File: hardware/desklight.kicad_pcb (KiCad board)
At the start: 2 copper layers, 30 x 30 mm, 10 parts, among them IC1 ATTINY10-TS, P1 AVR_TPI, P2 Pwr5V1500mA, P3 WS2812_CON, SW1 Rotary_Encoder_Switch

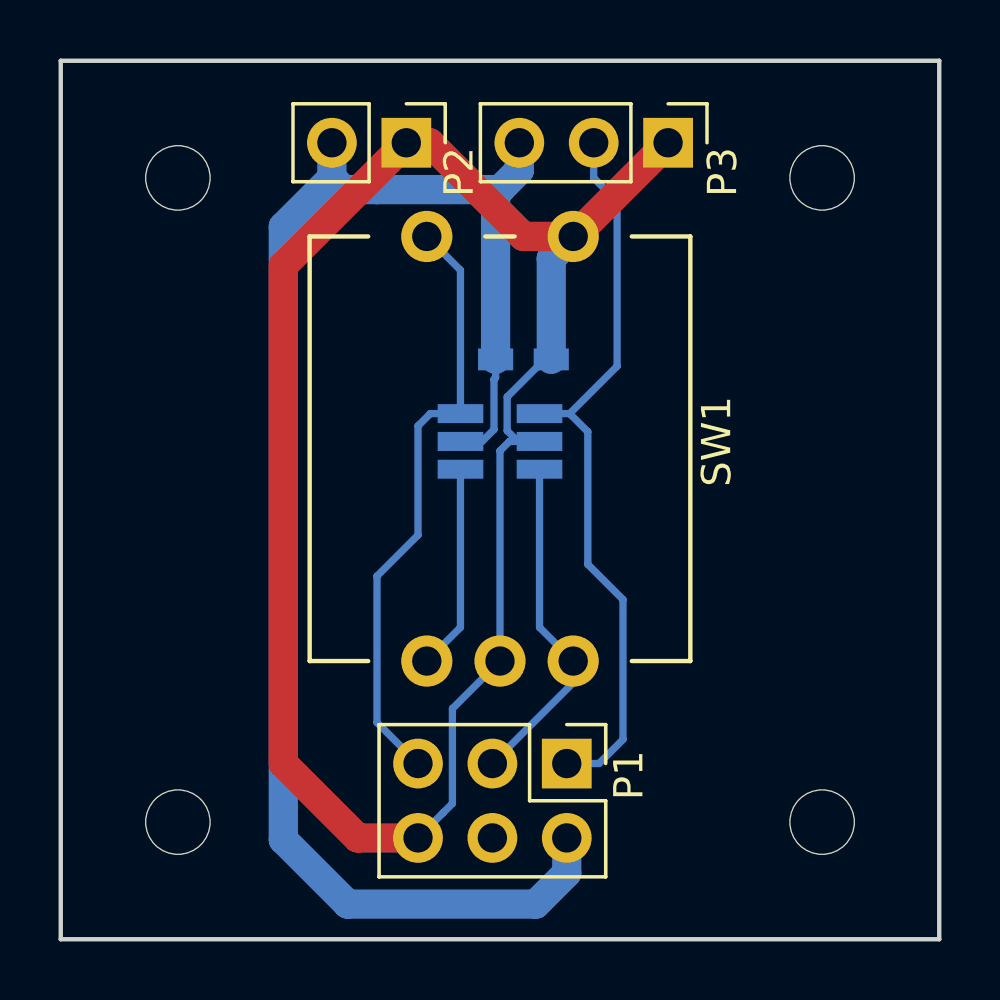
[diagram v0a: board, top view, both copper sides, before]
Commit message: add debouncing caps
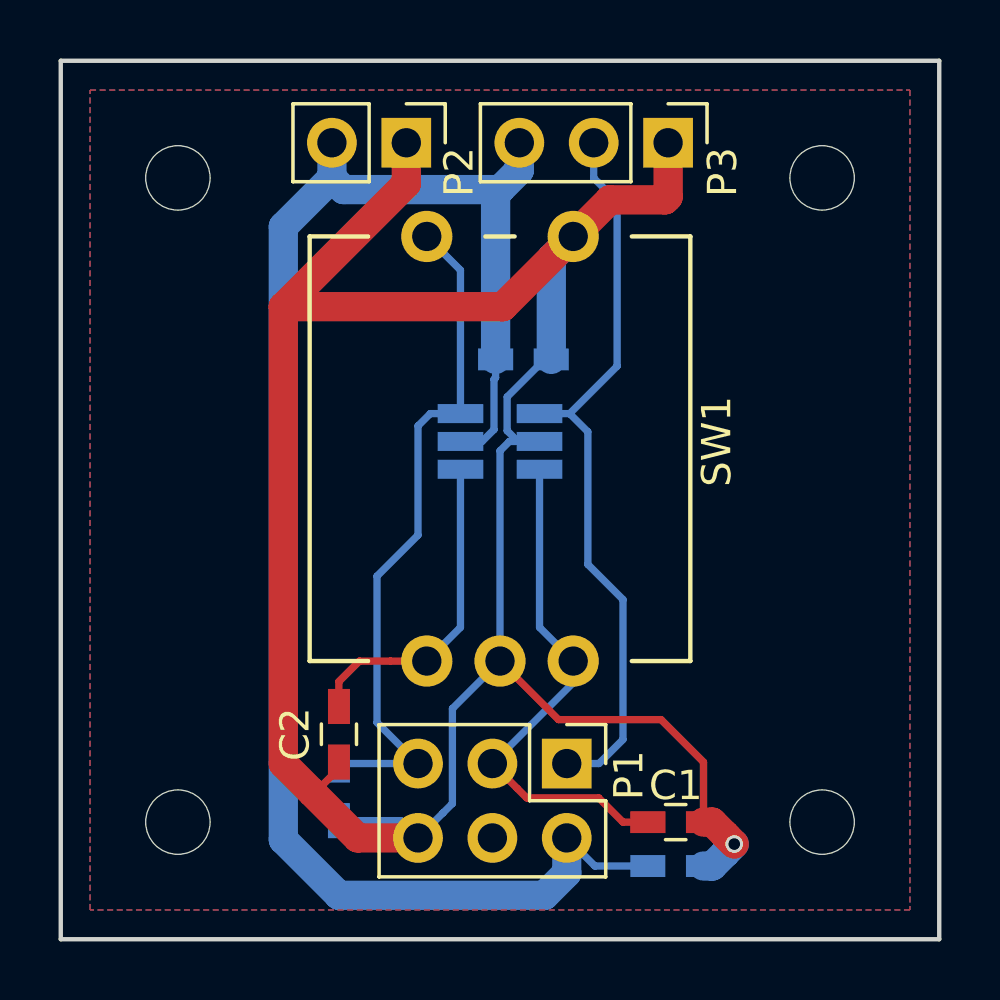
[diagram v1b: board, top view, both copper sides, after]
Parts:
- added C1: C, Capacitors_SMD:C_0603_HandSoldering, F.Cu at (151.0, 106.0)
- added C2: C, Capacitors_SMD:C_0603_HandSoldering, F.Cu at (139.5, 103.0)
- added C3: C, Capacitors_SMD:C_0603_HandSoldering, B.Cu at (139.5, 105.0)
- added C4: 100n, Capacitors_SMD:C_0603_HandSoldering, B.Cu at (151.0, 107.5)
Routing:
- net GND: track 65.0 -> 87.6 mm, vias 0 -> 1
- net /SCK: track 11.7 -> 17.8 mm
- net Net-(C2-Pad1): track 7.03 -> 11.2 mm
- net VCC: track 54.1 -> 57.0 mm
- net /~RESET: track 20.8 -> 23.6 mm
- added copper zone on B.Cu, net GND
- added copper zone on F.Cu, net GND

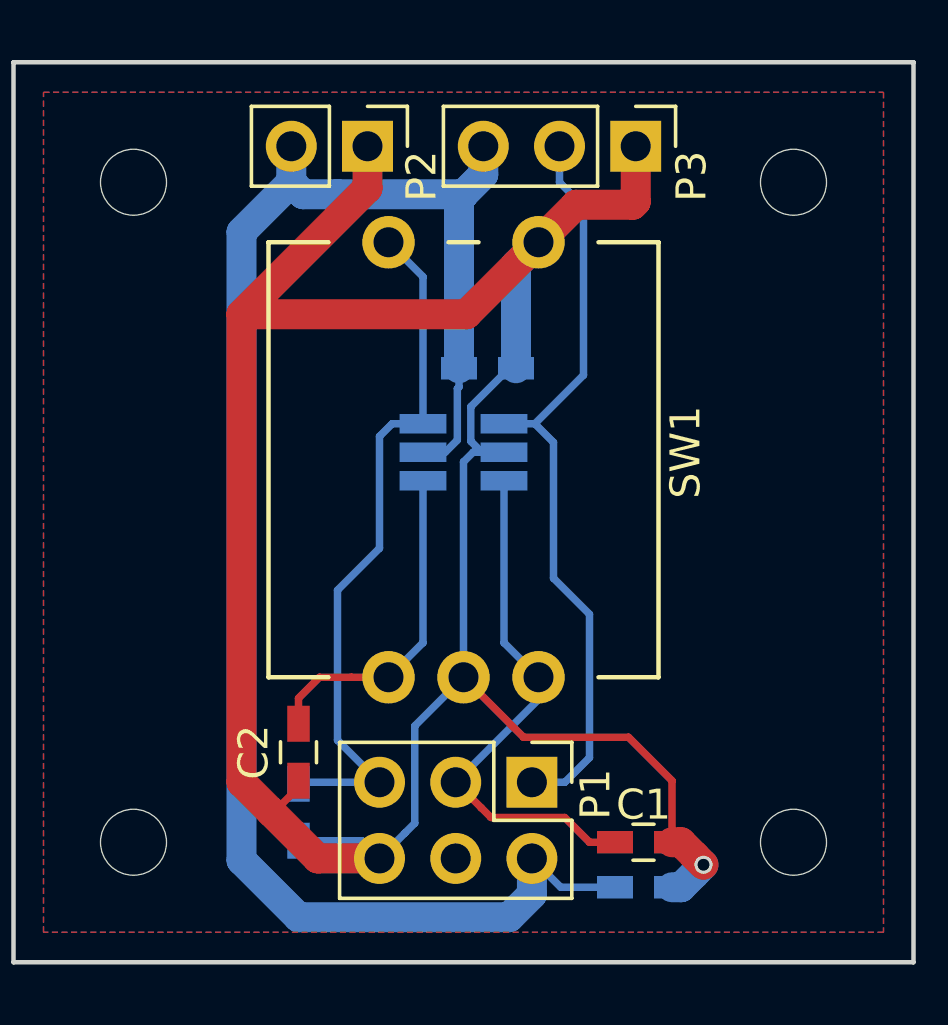
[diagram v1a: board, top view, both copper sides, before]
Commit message: re-routed with cleanup
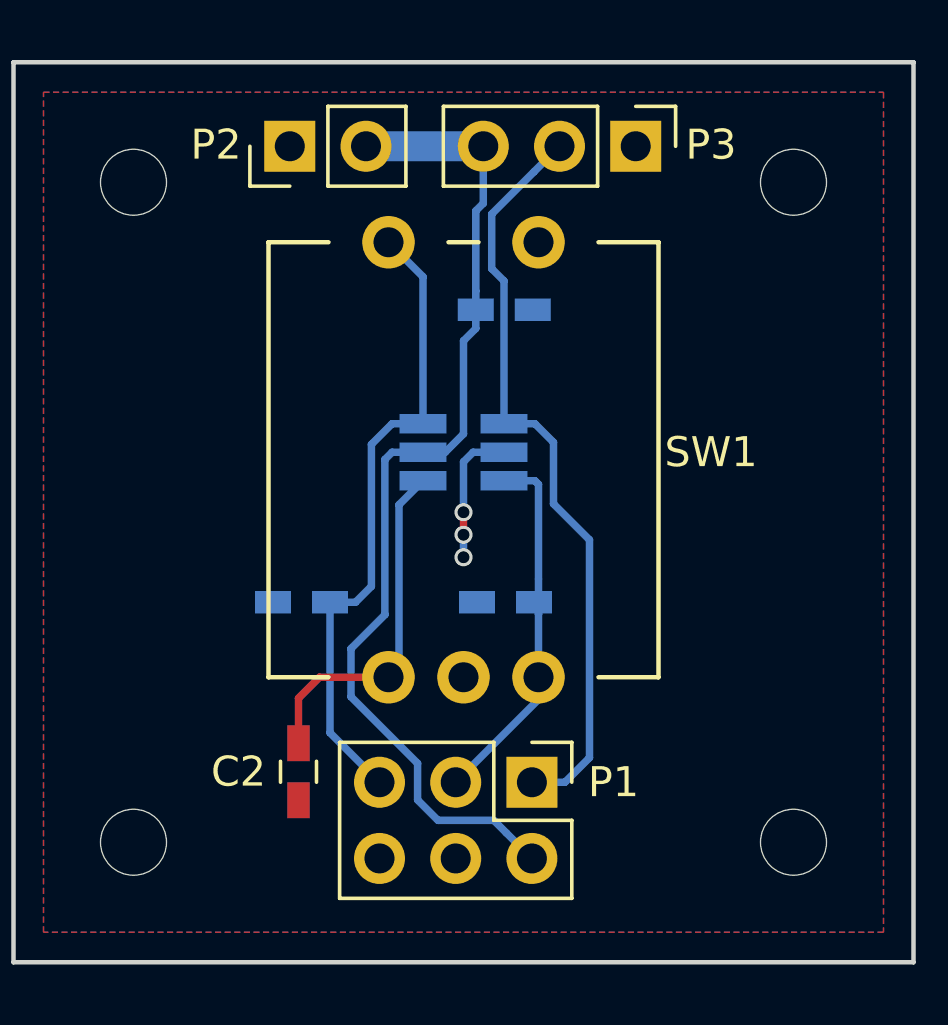
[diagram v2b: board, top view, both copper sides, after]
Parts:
- removed C5: 100n, Capacitors_SMD:C_0603_HandSoldering
- C1: moved to B.Cu
- moved C4 19.8 mm to (146.4, 88.2)
- moved C1 9.23 mm to (146.4, 98.0), turned to 180 degrees
- moved C3 7.00 mm to (139.6, 98.0), turned to 180 degrees
- moved P2 2.59 mm to (139.2, 82.8), turned to 90 degrees
- moved C2 0.65 mm to (139.5, 103.7)
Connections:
- P1 pad 4: Net-(P1-Pad4) -> (no net)
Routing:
- net GND: track 87.6 -> 4.70 mm, vias 1 -> 3
- net VCC: track 57.0 -> 34.1 mm
- net /SCK: track 17.8 -> 12.7 mm
- net /~RESET: track 23.6 -> 21.6 mm
- net Net-(C2-Pad1): track 11.2 -> 11.8 mm

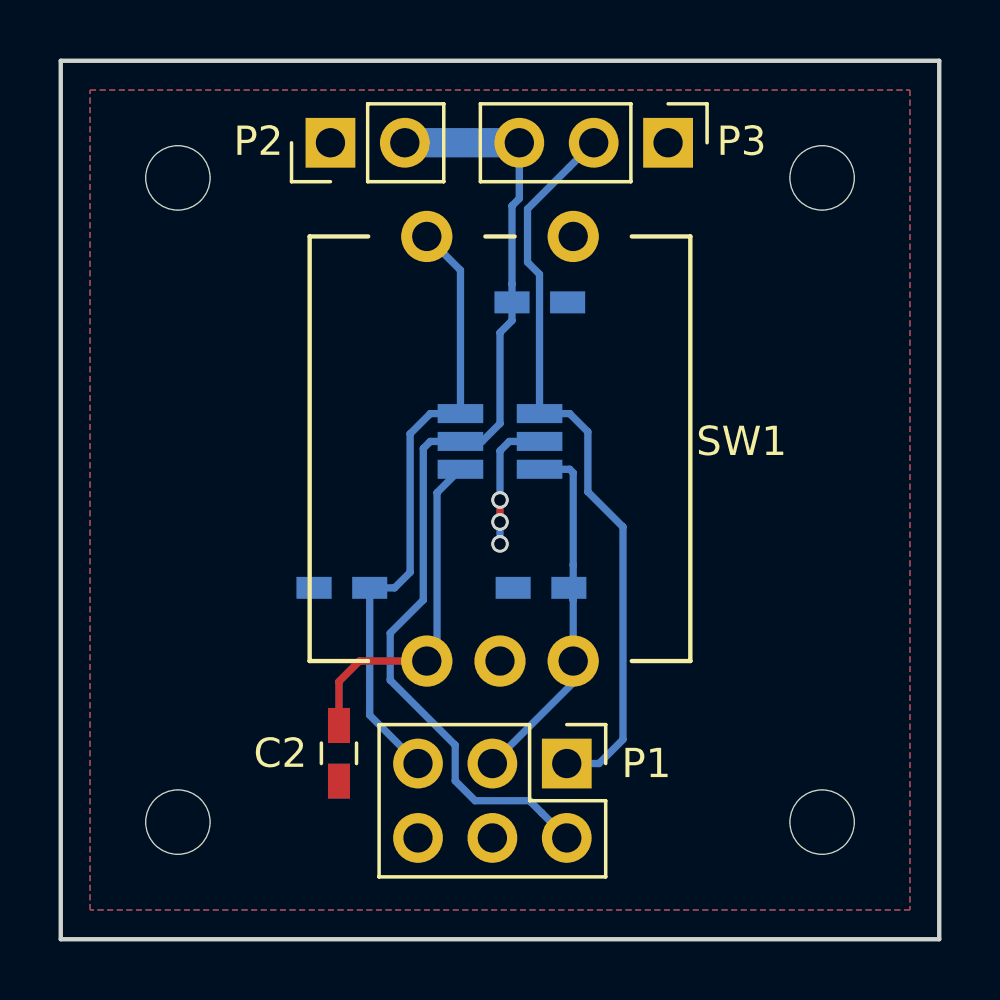
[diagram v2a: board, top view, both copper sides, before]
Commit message: re-route in 2.5x2.5cm formfactor.
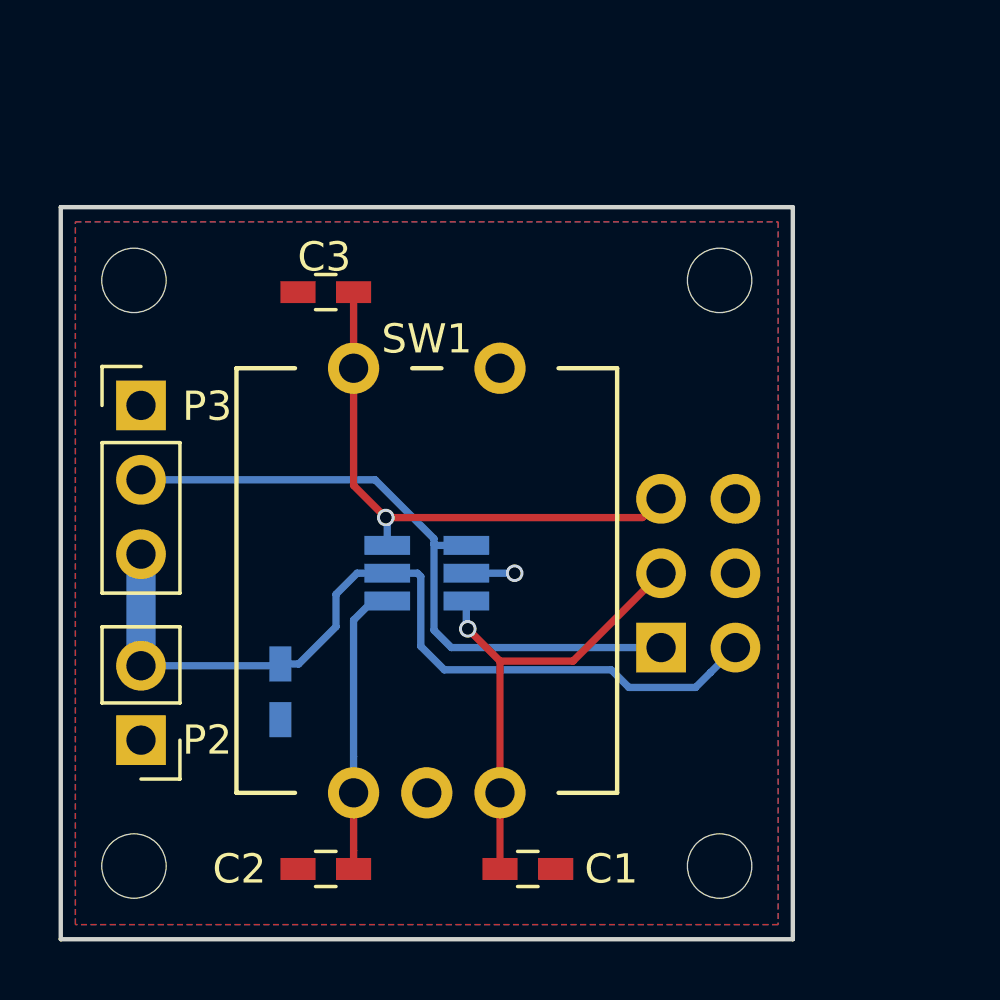
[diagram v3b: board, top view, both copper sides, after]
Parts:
- C1, C3: moved to F.Cu
- P1: moved to B.Cu
- moved P2 21.4 mm to (132.7, 103.2), turned to 180 degrees
- moved P3 20.1 mm to (132.7, 91.8), turned to 0 degrees
- moved C4 16.0 mm to (137.5, 101.5), turned to 270 degrees
- moved C3 10.1 mm to (139.1, 87.9)
- moved C1 9.61 mm to (145.9, 107.6), turned to 0 degrees
- moved IC1 5.15 mm to (142.5, 97.5)
- moved SW1 5.15 mm to (142.5, 97.5)
- moved P1 5.10 mm to (150.5, 100.0), turned to 0 degrees
- moved REF** 4.95 mm to (152.5, 87.5)
- moved C2 3.98 mm to (139.1, 107.6), turned to 180 degrees
- moved REF** 3.81 mm to (152.5, 107.5)
- moved REF** 3.81 mm to (132.5, 87.5)
- moved REF** 2.12 mm to (132.5, 107.5)
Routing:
- net VCC: track 34.1 -> 29.6 mm
- net /SCK: track 12.7 -> 16.8 mm, vias 0 -> 1
- net GND: track 4.70 -> 1.65 mm, vias 3 -> 1
- net /~RESET: track 21.6 -> 18.8 mm, vias 0 -> 1
- net /DOUT: track 25.8 -> 23.1 mm
- net Net-(C2-Pad1): track 11.8 -> 9.92 mm
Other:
- board size 30 x 30 mm -> 25 x 25 mm

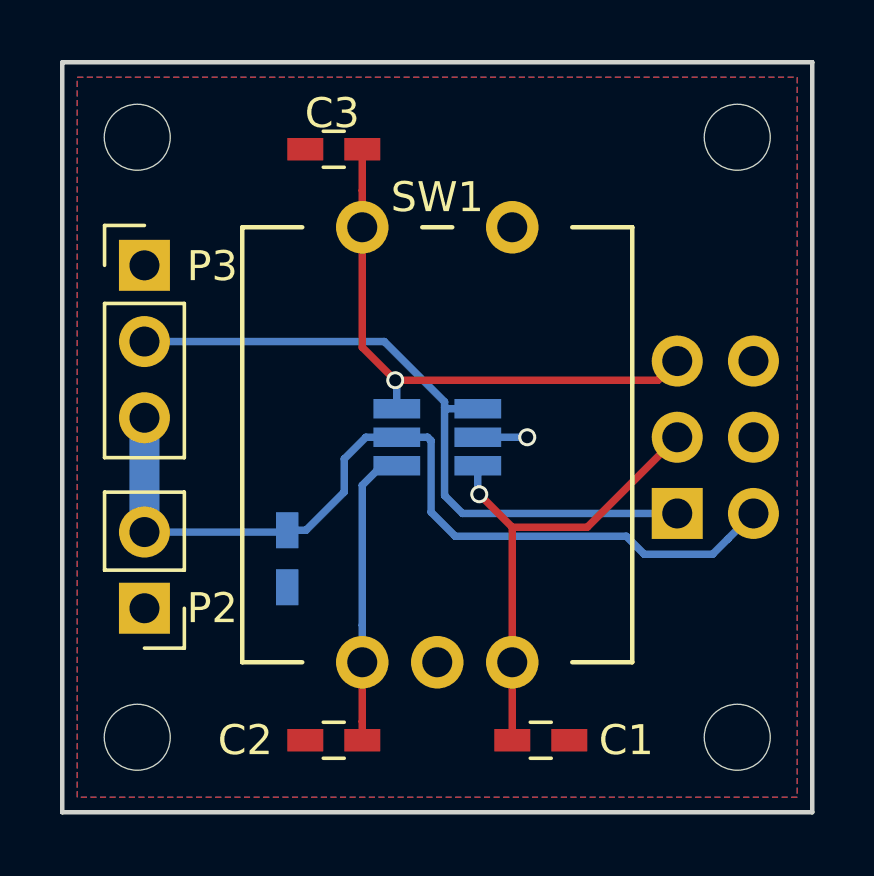
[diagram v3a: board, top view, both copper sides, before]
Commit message: added resistors to allow in-circuit programming
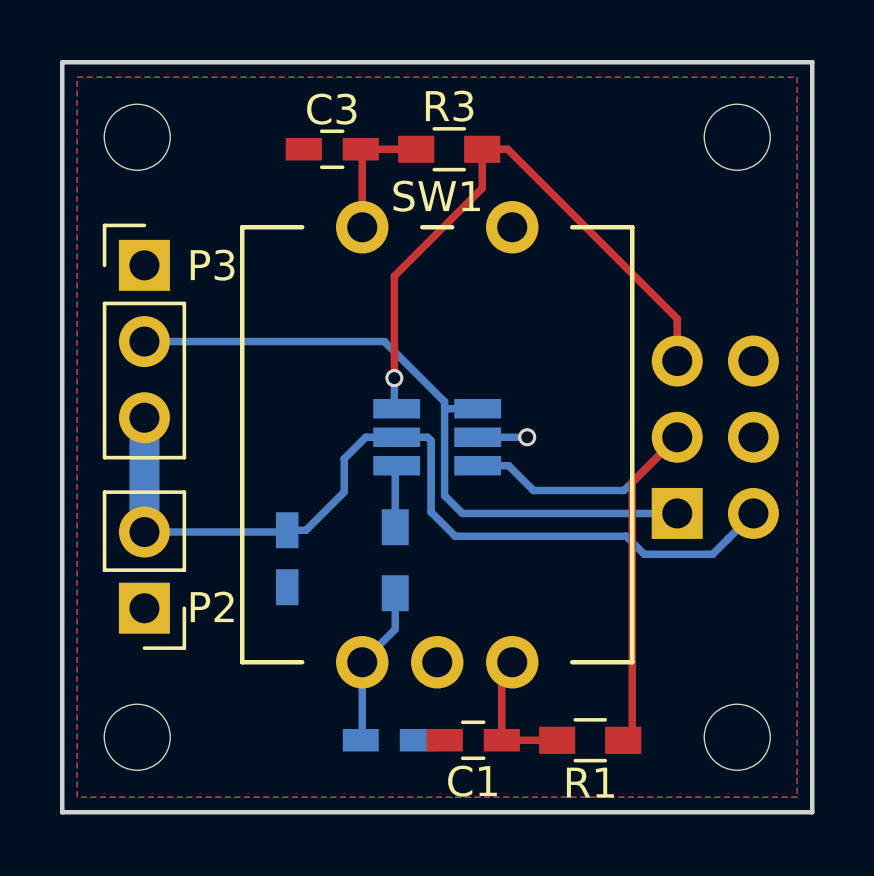
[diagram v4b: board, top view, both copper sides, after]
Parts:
- added R1: 1k, Resistors_SMD:R_0603_HandSoldering, F.Cu at (147.6, 107.6)
- added R2: 1k, Resistors_SMD:R_0603_HandSoldering, B.Cu at (141.1, 101.6)
- added R3: 1k, Resistors_SMD:R_0603_HandSoldering, F.Cu at (142.9, 87.9)
- C2: moved to B.Cu
- moved C1 2.25 mm to (143.7, 107.6), turned to 180 degrees
- moved C2 1.85 mm to (140.9, 107.6), turned to 0 degrees
- moved C3 0.05 mm to (139.0, 87.9)
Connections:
- C1 pad 1: /SCK -> Net-(C1-Pad1)
- C3 pad 1: /~RESET -> Net-(C3-Pad1)
- IC1 pad 4: Net-(C2-Pad1) -> Net-(IC1-Pad4)
- P1 pad 4: (no net) -> Net-(P1-Pad4)
- SW1 pad 3: /SCK -> Net-(C1-Pad1)
- SW1 pad 4: /~RESET -> Net-(C3-Pad1)
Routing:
- net Net-(C1-Pad1): track 0.00 -> 4.59 mm
- net Net-(C2-Pad1): track 9.92 -> 5.38 mm
- net Net-(C3-Pad1): track 0.00 -> 4.47 mm
- net /SCK: track 16.8 -> 19.0 mm, vias 1 -> 0
- net Net-(IC1-Pad4): track 0.00 -> 2.07 mm
- net /~RESET: track 18.8 -> 20.1 mm
